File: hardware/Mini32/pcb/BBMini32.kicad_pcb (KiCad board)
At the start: 2 copper layers, 100 x 70 mm, 39 parts, among them J1 POWER, Q1 S8550, SW1 SW_Push_Dual, SW2 SW_Push_Dual, U1 ESP-32_NodeMCU, U2 74HC595, U3 HD44780, U4 MCP3208

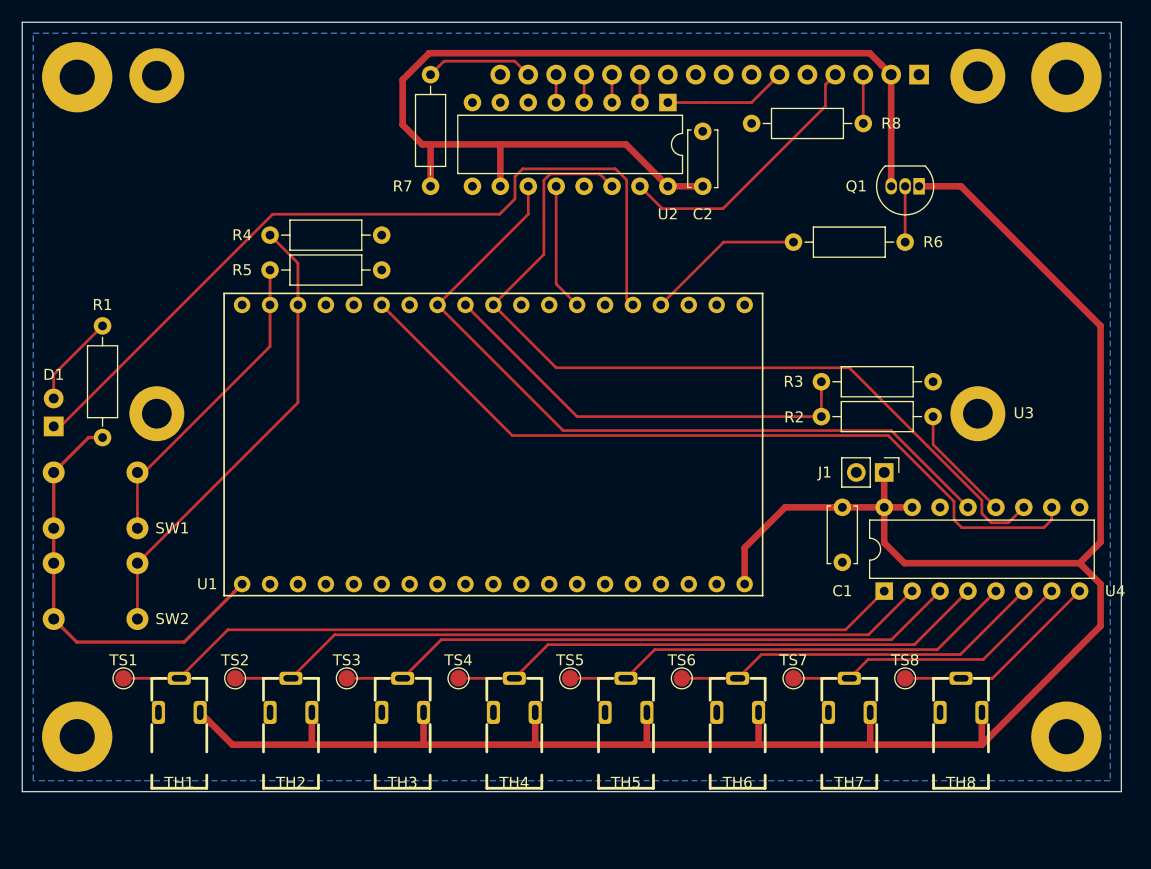
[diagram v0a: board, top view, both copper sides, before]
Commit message: feat: Split 5V rail from main PCB
shrink PCB

Issue #51
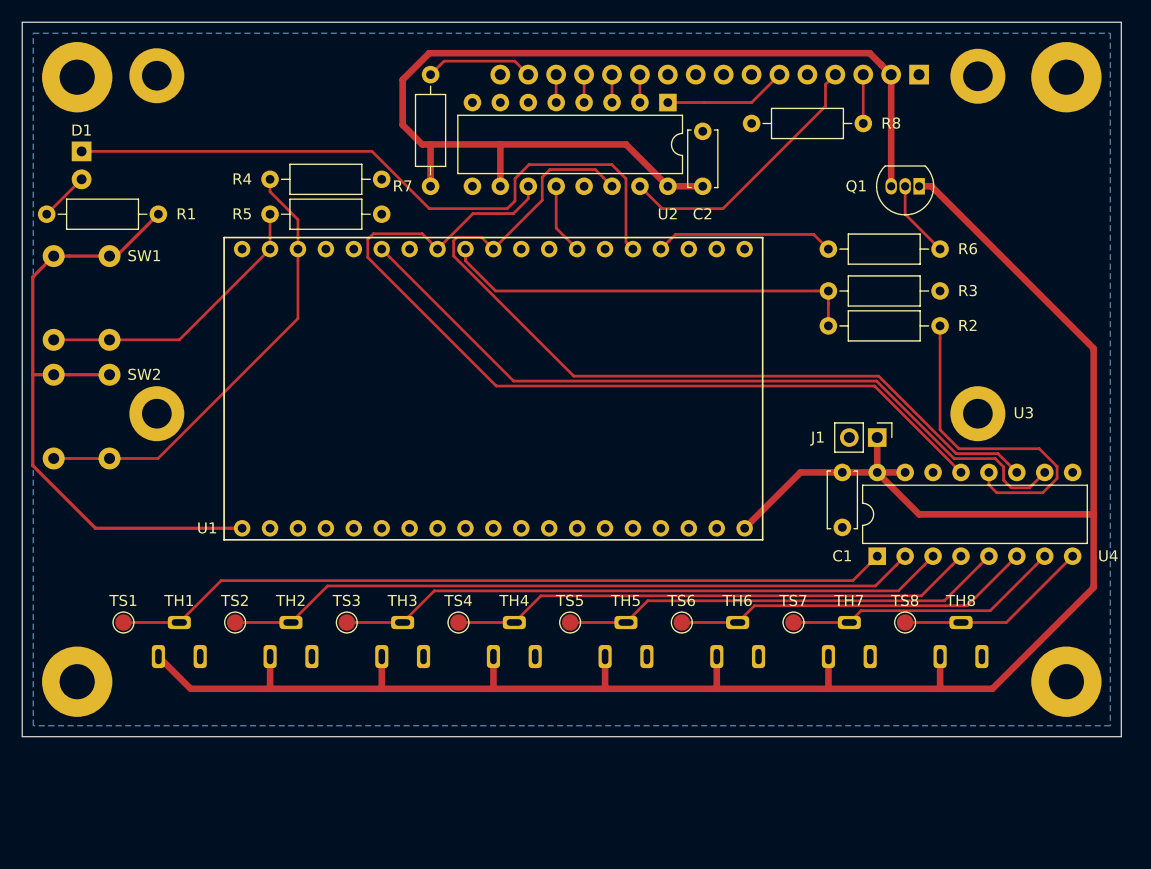
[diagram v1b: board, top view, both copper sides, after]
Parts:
- TH1, TH2, TH3, TH4, TH5, TH6, TH7, TH8: moved to B.Cu
- moved D1 25.1 mm to (25.4, 31.8), turned to 270 degrees
- moved R1 20.9 mm to (32.4, 37.5), turned to 180 degrees
- moved SW1 20.3 mm to (27.9, 41.3), turned to 270 degrees
- moved SW2 17.9 mm to (27.9, 52.1), turned to 270 degrees
- moved R2 8.28 mm to (103.5, 47.6)
- moved R3 8.28 mm to (93.3, 44.5)
- moved R4 5.08 mm to (42.5, 34.3)
- moved R5 5.08 mm to (42.5, 37.5)
- moved TH1 5.08 mm to (34.3, 84.6), turned to 0 degrees
- moved TH2 5.08 mm to (44.5, 84.6), turned to 0 degrees
- moved TH3 5.08 mm to (54.6, 84.6), turned to 0 degrees
- moved TH4 5.08 mm to (64.8, 84.6), turned to 0 degrees
- moved TH5 5.08 mm to (74.9, 84.6), turned to 0 degrees
- moved TH6 5.08 mm to (85.1, 84.6), turned to 0 degrees
- moved TH7 5.08 mm to (95.2, 84.6), turned to 0 degrees
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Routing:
- net /MISO: track 10.6 -> 30.7 mm
- net +3V3: track 39.3 -> 59.3 mm
- net Net-(D1-Pad1): track 75.1 -> 61.7 mm
- net /SCLK: track 70.1 -> 82.2 mm
- net +5V: track 203.8 -> 195.6 mm
- net /CS2: track 11.6 -> 6.50 mm
- net Net-(D1-Pad2): track 8.45 -> 4.49 mm
- net /MOSI: track 77.9 -> 80.6 mm
- net Net-(R5-Pad1): track 28.8 -> 26.3 mm
- net Net-(Q1-Pad2): track 5.08 -> 7.03 mm
- net Net-(R6-Pad1): track 14.4 -> 16.3 mm
- net /SIGNAL4: track 49.6 -> 48.2 mm
- net /SIGNAL8: track 19.2 -> 17.7 mm
- net /SIGNAL6: track 34.4 -> 33.0 mm
- net /SIGNAL2: track 64.9 -> 63.5 mm
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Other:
- board size 100 x 70 mm -> 100 x 65 mm
- net class 3V3: clearance 0.3 -> 0.2
- net class Default: clearance 0.2 -> 0.1
- rule trace_clearance: 0.2 -> 0.1

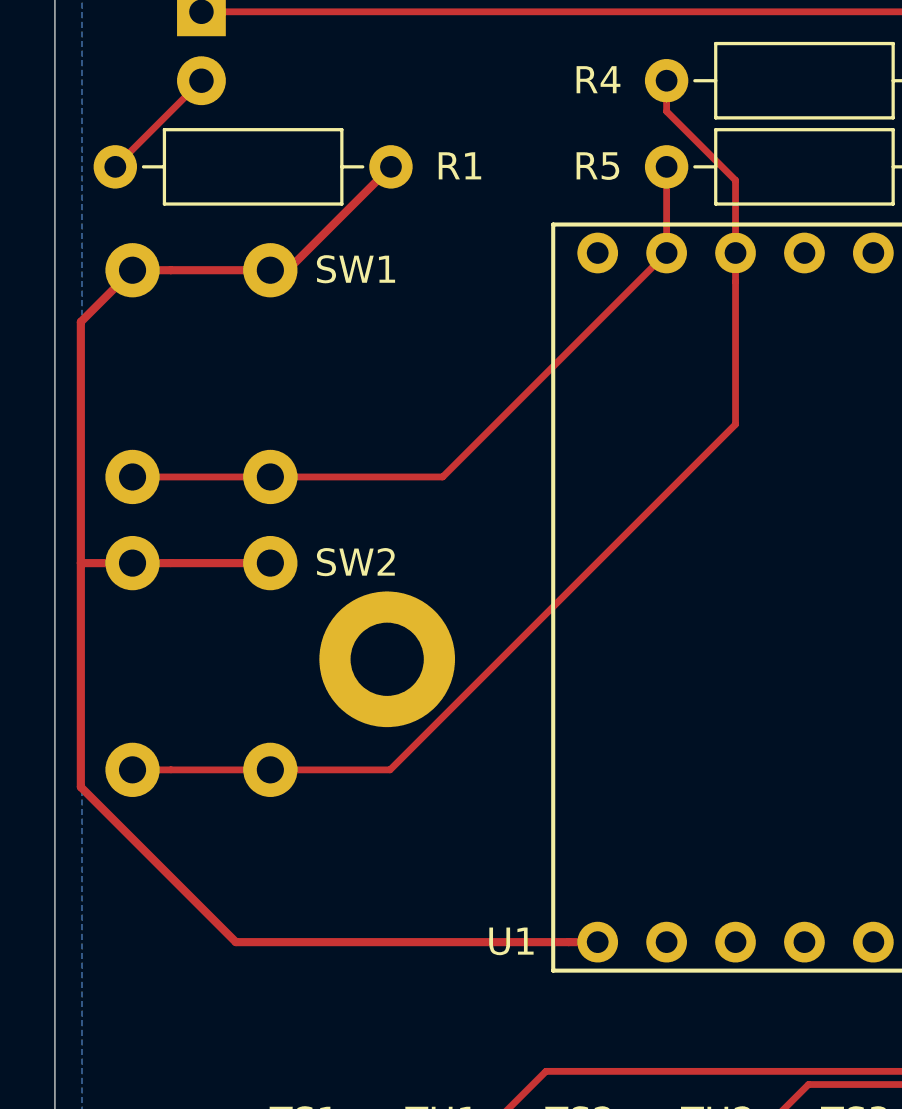
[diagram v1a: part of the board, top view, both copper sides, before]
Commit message: feat: Split 5V rail from main PCB
shrink pcp, switch push buttons

Issue #51
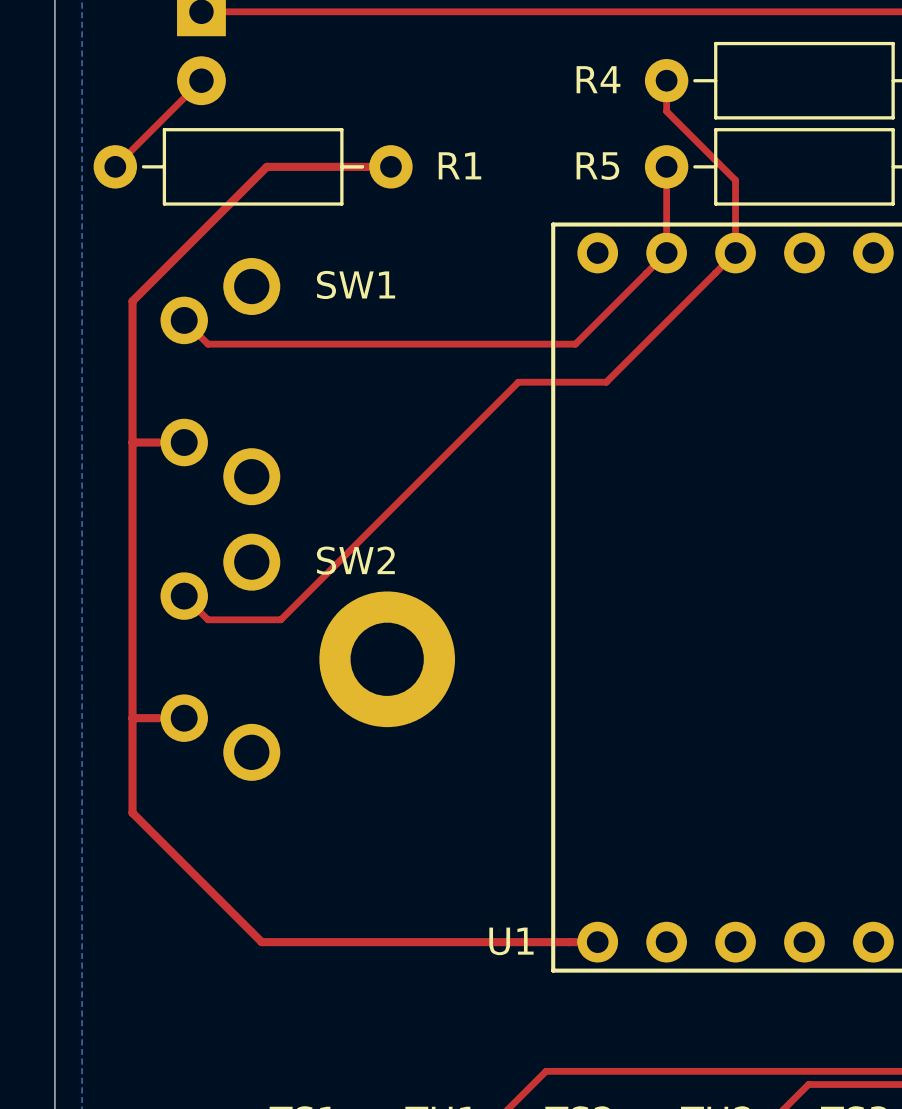
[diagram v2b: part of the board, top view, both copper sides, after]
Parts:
- SW1, SW2: value SW_Push_Dual -> SW_Push; footprint NAMAE:NAMAE_JTP-1130P -> Button_Switch_THT:SW_Tactile_SPST_Angled_PTS645Vx31-2LFS
- moved SW1 3.67 mm to (24.8, 43.1)
- moved SW2 3.40 mm to (24.8, 53.3)
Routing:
- net Net-(R4-Pad1): track 41.2 -> 33.7 mm
- net +3V3: track 59.3 -> 53.4 mm
- net Net-(R5-Pad1): track 26.3 -> 22.7 mm

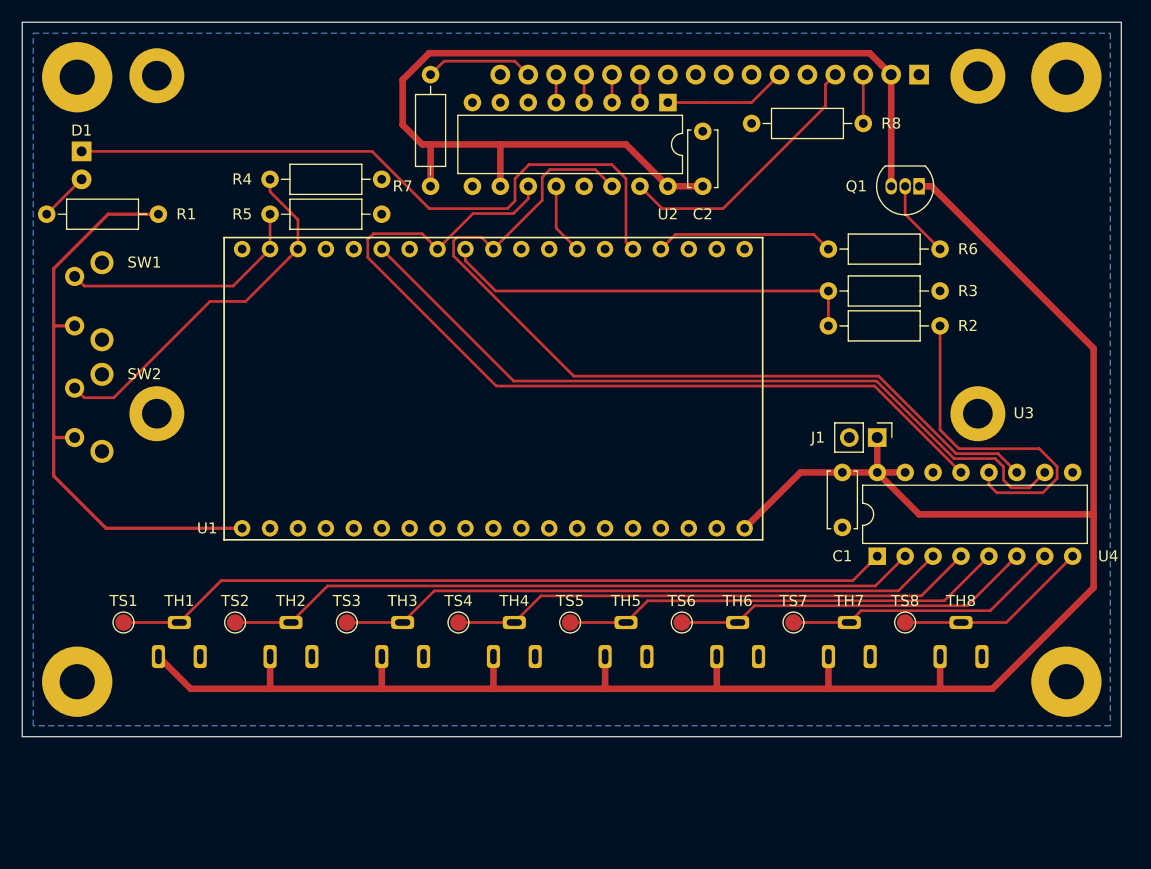
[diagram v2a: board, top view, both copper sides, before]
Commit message: feat: Split 5V rail from main PCB
redo PCB

Issue #51
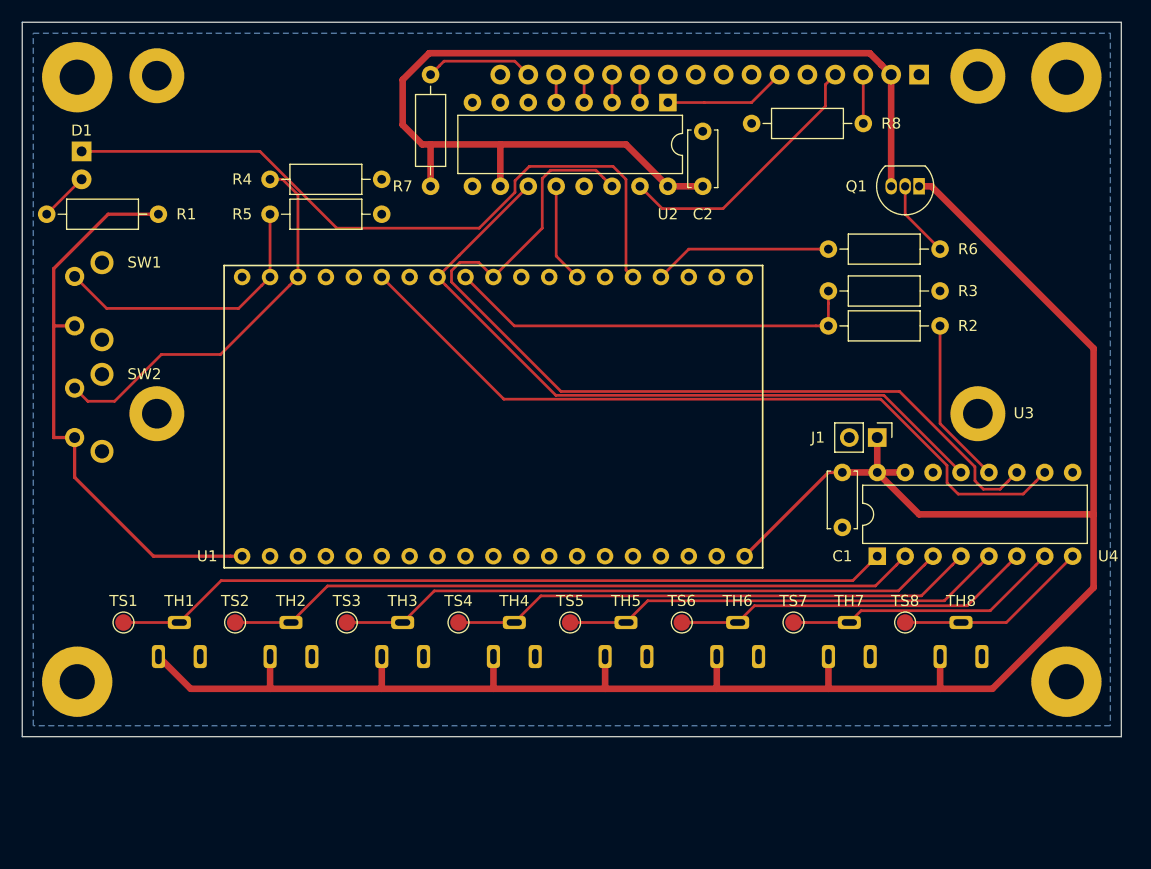
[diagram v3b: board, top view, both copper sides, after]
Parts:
- moved U1 2.54 mm to (62.9, 55.9)
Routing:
- net /MISO: track 30.7 -> 15.2 mm
- net /SCLK: track 82.2 -> 66.7 mm
- net /MOSI: track 80.6 -> 84.4 mm
- net Net-(D1-Pad1): track 61.7 -> 65.0 mm
- net Net-(R5-Pad1): track 22.7 -> 25.9 mm
- net /CS2: track 6.50 -> 9.04 mm
- net Net-(R4-Pad1): track 33.7 -> 36.1 mm
- net +5V: track 195.6 -> 196.6 mm
- net +3V3: track 53.4 -> 52.6 mm

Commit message: feat: Split 5V rail from main PCB
redo PCB, start lid

Issue #51
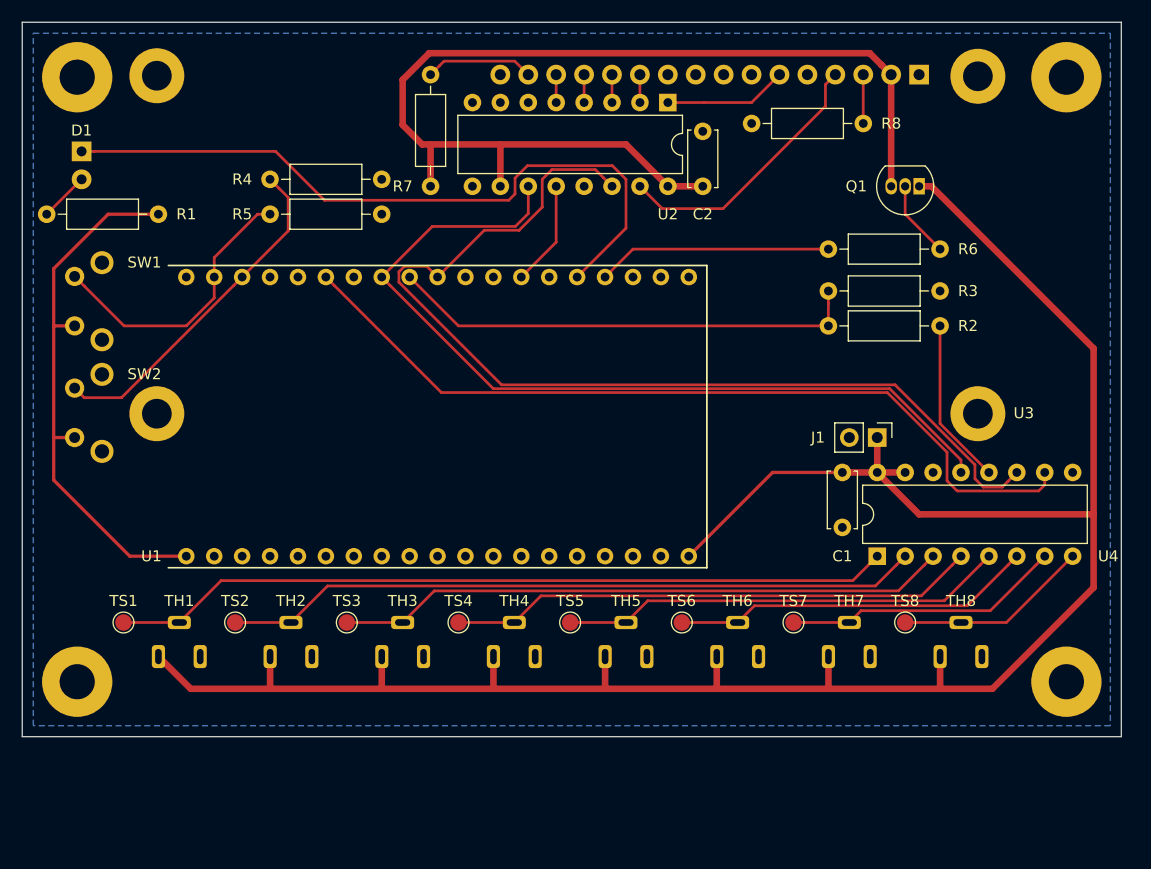
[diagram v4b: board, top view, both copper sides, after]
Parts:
- moved U1 5.08 mm to (57.8, 55.9)
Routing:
- net /SCLK: track 66.7 -> 78.9 mm
- net /MOSI: track 84.4 -> 92.3 mm
- net /CS1: track 70.3 -> 76.4 mm
- net +5V: track 196.6 -> 201.7 mm
- net /MISO_5V: track 38.0 -> 43.1 mm
- net Net-(R6-Pad1): track 16.3 -> 21.4 mm
- net Net-(R4-Pad1): track 36.1 -> 31.5 mm
- net +3V3: track 52.6 -> 49.6 mm
- net /CS2: track 9.04 -> 9.57 mm

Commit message: feat Firmware: Convert Temperatures
fix display relay with PNP/NPN combo

Issue #27
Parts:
- added Q2: S8050, Package_TO_SOT_THT:TO-92_Inline, F.Cu at (92.7, 35.6)
- R6: value 2k2 -> 270
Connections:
- R6 pad 1: Net-(R6-Pad1) -> Net-(Q2-Pad1)
- R6 pad 2: Net-(Q1-Pad2) -> GND
- U1 pad 35: Net-(R6-Pad1) -> Net-(Q2-Pad2)
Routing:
- net Net-(Q2-Pad2): track 0.00 -> 26.8 mm
- net Net-(R6-Pad1): track 21.4 -> 0.00 mm
- net Net-(Q2-Pad1): track 0.00 -> 5.34 mm

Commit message: feat: Firmware: Convert Temperatures
redo PCB with new Transistors

Issue #27
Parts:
- moved TH1 71.1 mm to (105.4, 84.6)
- moved TH8 71.1 mm to (34.3, 84.6)
- moved TS1 71.1 mm to (100.3, 74.6)
- moved TS8 71.1 mm to (29.2, 74.6)
- moved TS2 50.8 mm to (90.2, 74.6)
- moved TS7 50.8 mm to (39.4, 74.6)
- moved TH2 50.8 mm to (95.2, 84.6)
- moved TH7 50.8 mm to (44.5, 84.6)
- moved TH3 30.5 mm to (85.1, 84.6)
- moved TH6 30.5 mm to (54.6, 84.6)
- moved TS3 30.5 mm to (80.0, 74.6)
- moved TS6 30.5 mm to (49.5, 74.6)
- moved J1 24.3 mm to (106.0, 34.9), turned to 90 degrees
- moved TH4 10.2 mm to (74.9, 84.6)
- moved TH5 10.2 mm to (64.8, 84.6)
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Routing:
- net /SIGNAL8: track 17.7 -> 90.4 mm
- net /SIGNAL1: track 71.1 -> 11.5 mm
- net /SIGNAL7: track 25.4 -> 78.0 mm
- net /SIGNAL2: track 63.5 -> 16.2 mm
- net /SIGNAL6: track 33.0 -> 65.7 mm
- net /SIGNAL3: track 55.8 -> 28.6 mm
- net +5V: track 201.7 -> 176.8 mm
- net /MOSI: track 92.3 -> 77.4 mm
- net /SIGNAL5: track 40.6 -> 53.3 mm
- net /SCLK: track 78.9 -> 70.1 mm
- net /SIGNAL4: track 48.2 -> 40.9 mm
- net /CS1: track 76.4 -> 70.1 mm
- net Net-(R4-Pad1): track 31.5 -> 26.8 mm
- net /VDISP: track 97.8 -> 100.9 mm
- net Net-(D1-Pad1): track 64.8 -> 67.3 mm
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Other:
- net class Default: clearance 0.1 -> 0.15
- rule trace_clearance: 0.1 -> 0.15
